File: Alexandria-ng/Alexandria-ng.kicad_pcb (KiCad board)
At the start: 4 copper layers, 150 x 105 mm, 87 parts, among them J1 Eth0, J10 PoE3, J11 PoE4, J12 FFC, J13 +3.3V, J14 I²C, J2 Eth1, J3 Eth2, J4 Eth3, J5 Eth4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

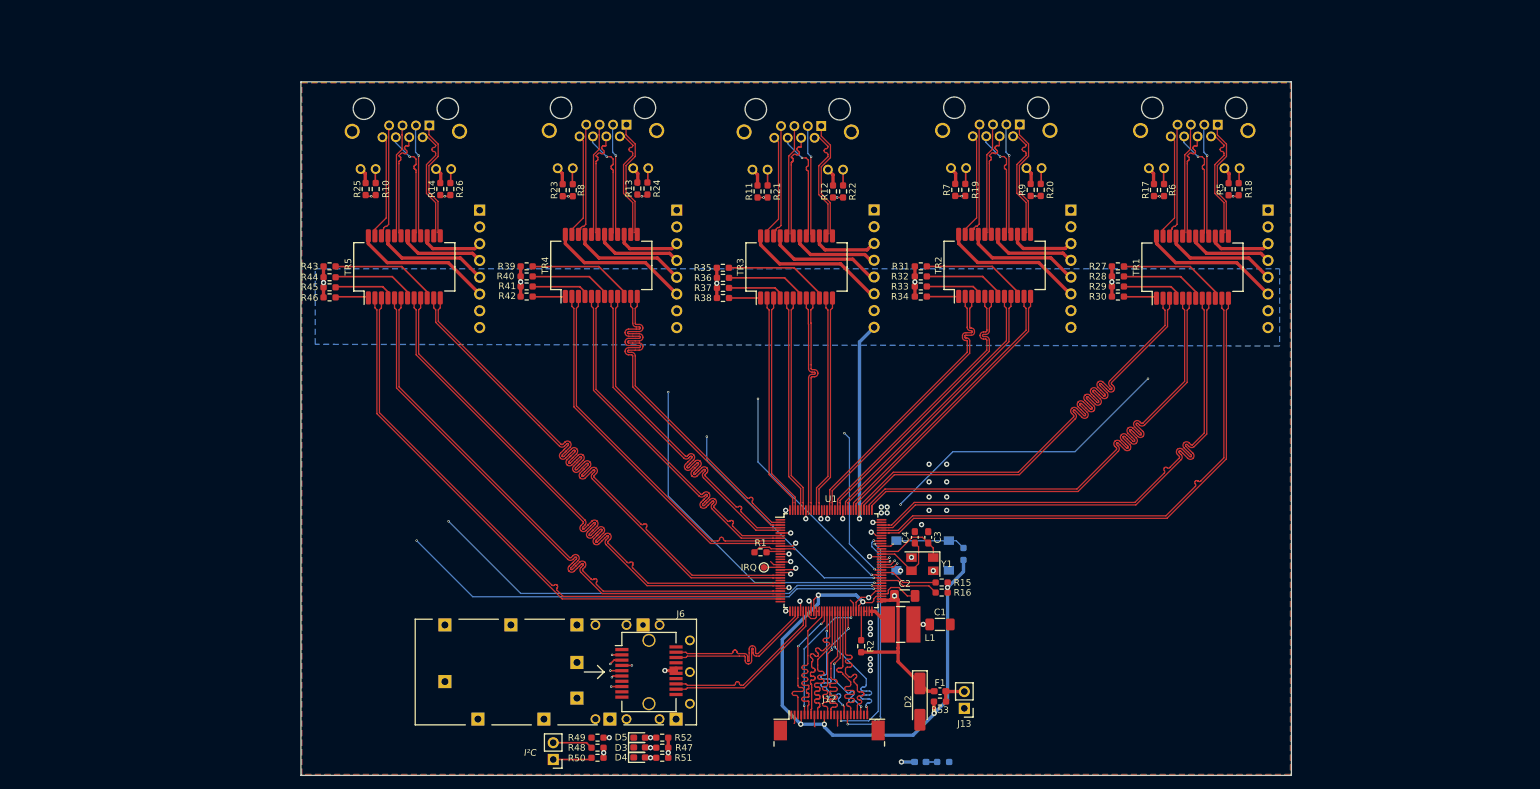
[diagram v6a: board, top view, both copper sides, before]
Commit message: Added GND vias
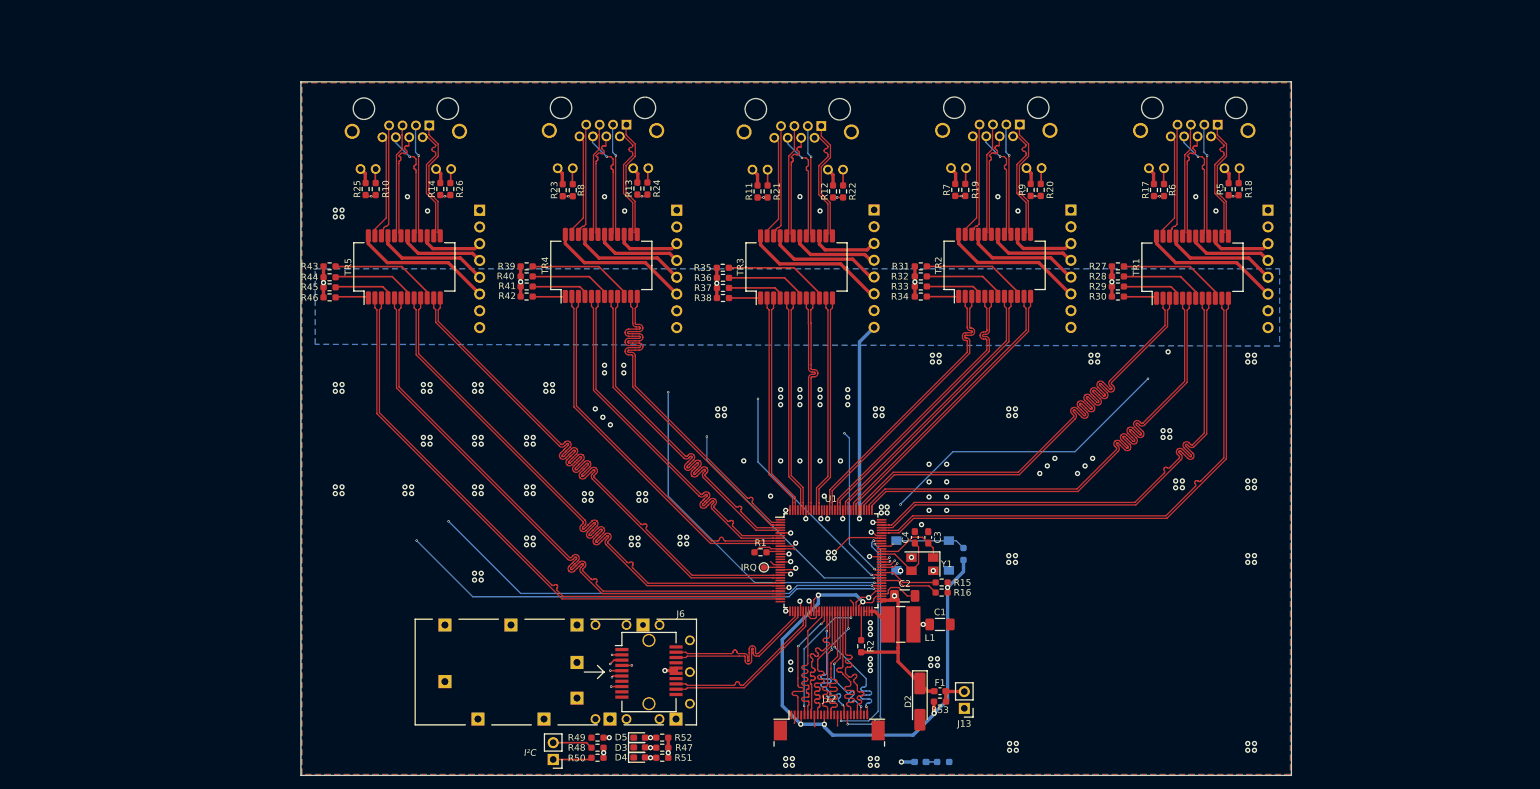
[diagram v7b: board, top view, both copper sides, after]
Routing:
- net GND: track 32.3 -> 40.4 mm, vias 22 -> 208
